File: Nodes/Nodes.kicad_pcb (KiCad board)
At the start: 4 copper layers, 84.8 x 75 mm, 295 parts, among them IC1 VNQ9025AJTR, IC2 VNQ9025AJTR, IC3 TCAN1462VDRQ1, IC4 TCAN1462VDRQ1, IC5 ST730MR, IC6 ST730MR, J1 Conn_01x04, J10 Conn_01x08, J11 Conn_01x08, J12 Conn_01x08, J13 Conn_01x08, J14 Conn_01x08, J2 Conn_01x04, J7 HLE-104-02-L-DV-BE-A-P-TR, J8 HLE-104-02-L-DV-BE-A-P-TR, J9 Conn_01x08, Q1 TN2106K1-G, Q2 TN2106K1-G, SW1 CJS-1201TB1, SW2 CJS-1201TB1, SW3 CAS-220TB1, T1 Conn_01x01, T10 Conn_01x01, T11 Conn_01x01, T12 Conn_01x01, T13 Conn_01x01, T14 Conn_01x01, T15 Conn_01x01, T16 Conn_01x01, T17 Conn_01x01, T18 Conn_01x01, T19 Conn_01x01, T2 Conn_01x01, T20 Conn_01x01, T21 Conn_01x01, T22 Conn_01x01, T23 Conn_01x01, T3 Conn_01x01, T4 Conn_01x01, T5 Conn_01x01, T6 Conn_01x01, T7 Conn_01x01, T8 Conn_01x01, T9 Conn_01x01, U1 STM32G431KBT6, U10 LM358BAIDR, U11 STM32G431RBTx, U5 LM358BAIDR, U6 LM358BAIDR, U7 LM358BAIDR, U8 LM358BAIDR, U9 LM358BAIDR, Y1 SG-8018CE_8.0000M-TJHPA3, Y2 SG-8018CE_8.0000M-TJHPA3

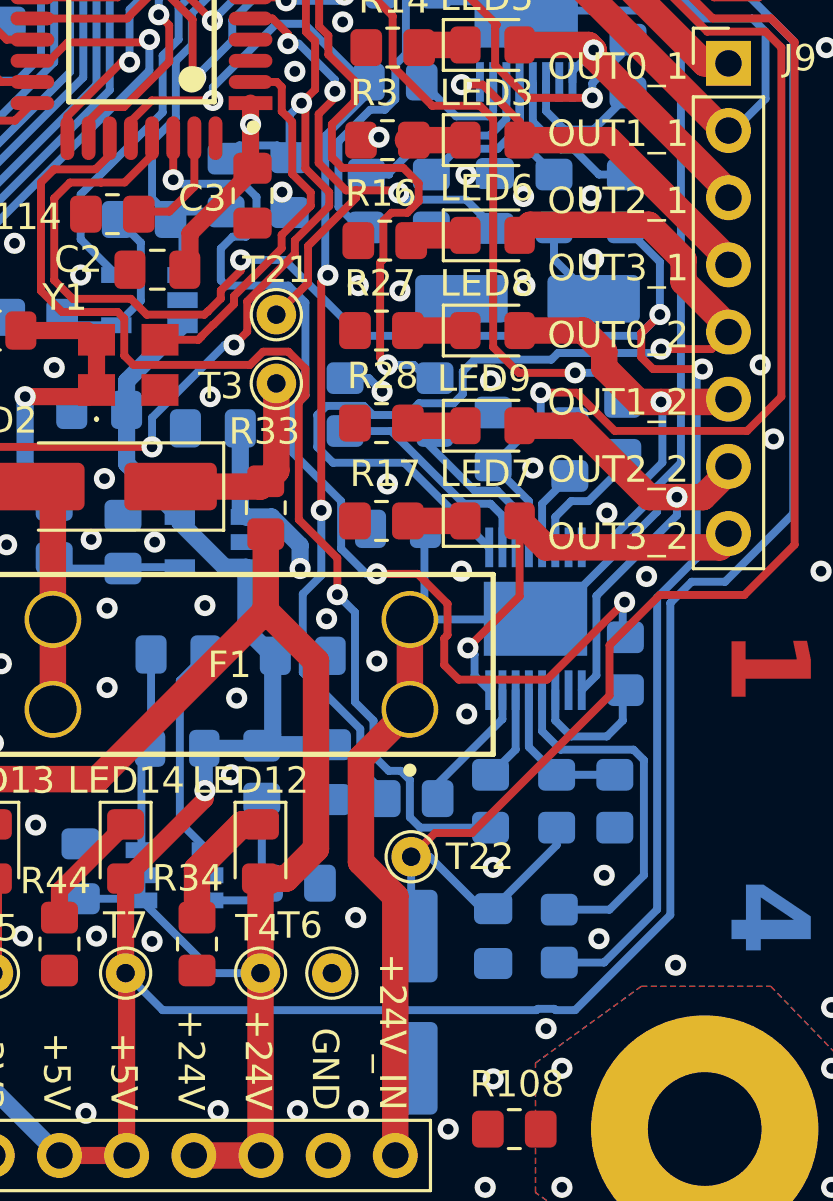
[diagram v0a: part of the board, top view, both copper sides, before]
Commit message: Nodes 2.2.5 Revision 1
- New LED colour coding
- Nodes Datasheet added
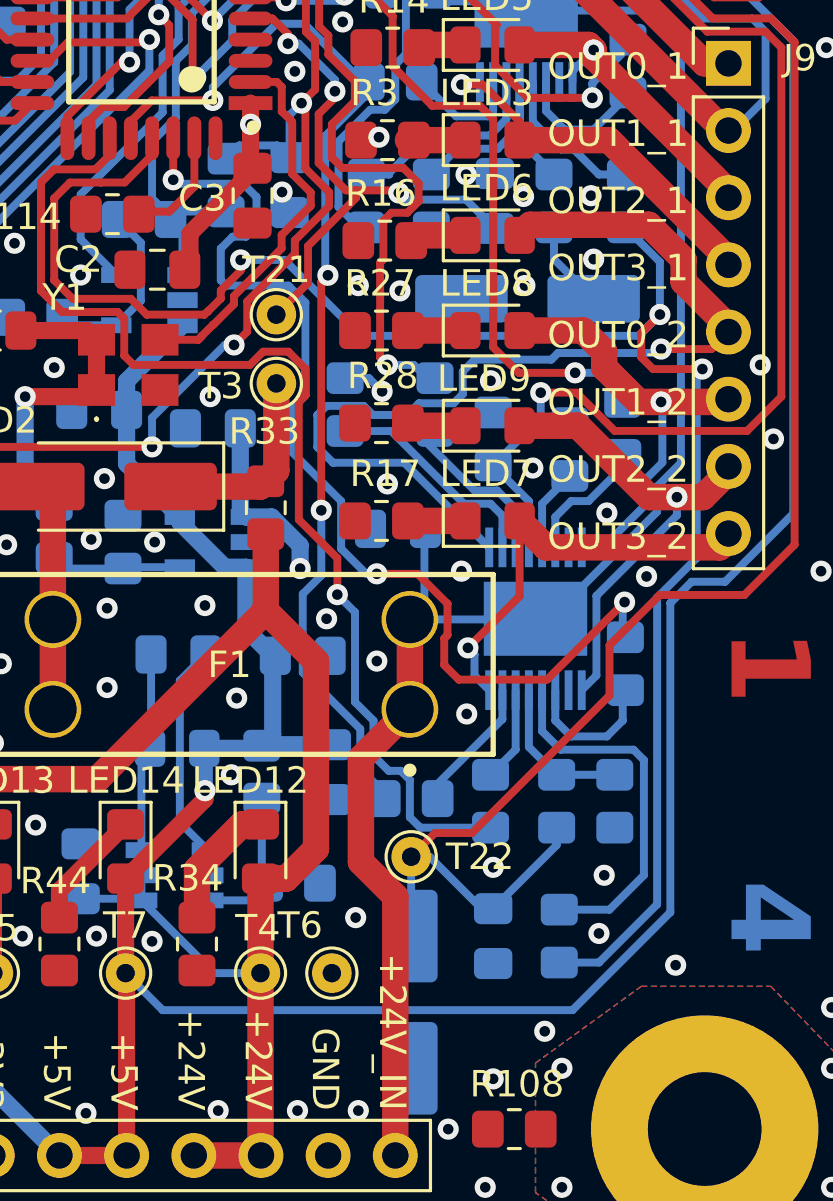
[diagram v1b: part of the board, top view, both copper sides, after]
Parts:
- LED1: value SML-210VTT86 -> SML-210YTT86M
- LED10: value SML-210VTT86 -> SML-H12P8TT86
- LED11: value SML-210VTT86 -> SML-H12D8TT86
- LED12: value SMLMN2WB1CW1 -> SML-210VTT86
- LED2, LED6: value SML-H12D8TT86 -> SML-210VTT86
- LED3, LED7: value 150080BS75000 -> SMLMN2WB1CW1
- LED4, LED8: value SML-210YTT86M -> SMLMN2WB1CW1
- LED5, LED9: value SML-H12P8TT86 -> SML-210VTT86
- R15, R29: value 1kR -> 2.2kR
- turned R15 to 90 degrees
- turned R29 to 90 degrees
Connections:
- R15 pad 1: Net-(IC1-CS) -> GND
- R15 pad 2: GND -> Net-(IC1-CS)
- R29 pad 1: Net-(IC2-CS) -> GND
- R29 pad 2: GND -> Net-(IC2-CS)
